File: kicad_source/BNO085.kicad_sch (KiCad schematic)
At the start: 16 parts, among them U4 BNO085, Y2 DNI

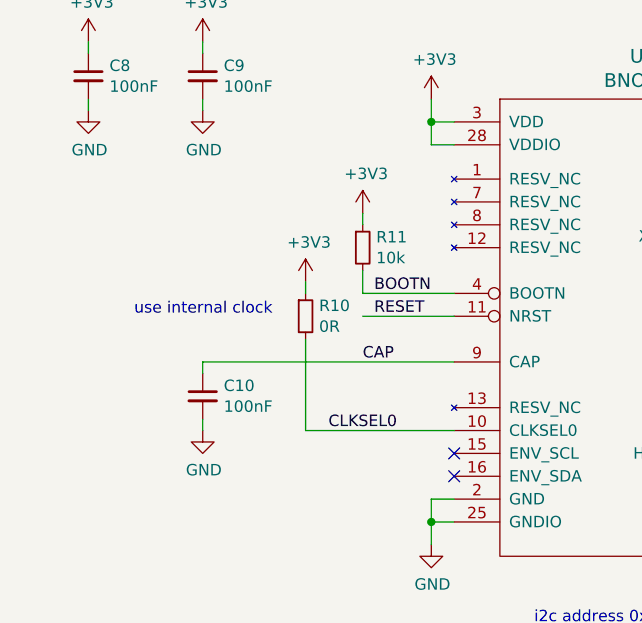
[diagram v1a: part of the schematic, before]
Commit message: connected reset of BNO055 and GNSS module, updated layout
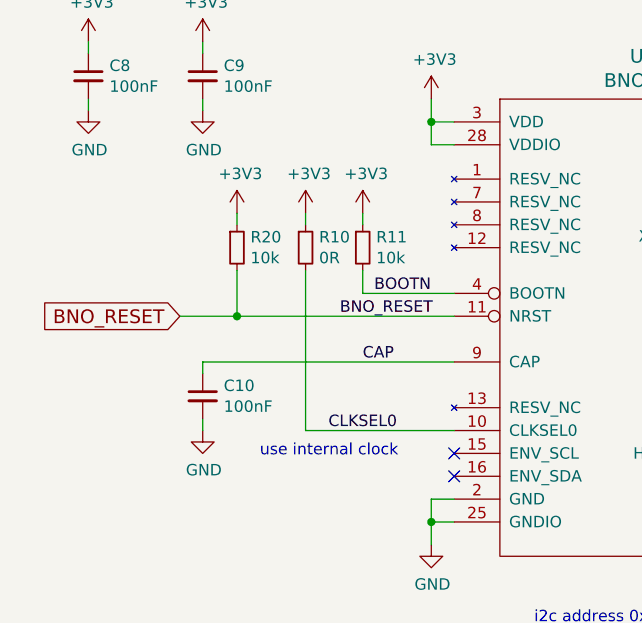
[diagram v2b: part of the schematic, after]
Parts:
- added R20: 10k, Resistor_SMD:R_0603_1608Metric, symbol NavShieldBNO-rescue:R_0603-devices
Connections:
- net +3V3: now also R20.1
- net RESET renamed BNO_RESET
- net BNO_RESET: now also R20.2
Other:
- moved on the sheet: R10
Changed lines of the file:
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@@
+	)
+	(junction
+		(at 39.37 54.61)
+		(diameter 0)
+		(color 0 0 0 0)
 	)
 	(junction
@@
 	(wire
 		(pts
+			(xy 39.37 49.53) (xy 39.37 54.61)
+		)
+		(stroke
+			(width 0)
+			(type default)
+		)
+	)
+	(wire
+		(pts
 			(xy 154.94 95.25) (xy 154.94 96.52)
 		)
@@
 	(wire
 		(pts
-			(xy 46.99 52.07) (xy 46.99 50.8)
+			(xy 46.99 44.45) (xy 46.99 43.18)
 		)
 		(stroke
@@
 	(wire
 		(pts
+			(xy 33.02 54.61) (xy 39.37 54.61)
+		)
+		(stroke
+			(width 0)
+			(type default)
+		)
+	)
+	(wire
+		(pts
 			(xy 140.97 59.69) (xy 140.97 72.39)
 		)
@@
 	(wire
 		(pts
+			(xy 39.37 54.61) (xy 63.5 54.61)
+		)
+		(stroke
+			(width 0)
+			(type default)
+		)
+	)
+	(wire
+		(pts
 			(xy 132.08 36.83) (xy 134.62 36.83)
 		)
@@
 	(wire
 		(pts
+			(xy 39.37 43.18) (xy 39.37 44.45)
+		)
+		(stroke
+			(width 0)
+			(type default)
+		)
+	)
+	(wire
+		(pts
 			(xy 154.94 101.6) (xy 154.94 102.87)
 		)
@@
 	(wire
 		(pts
-			(xy 53.34 54.61) (xy 63.5 54.61)
-		)
-		(stroke
-			(width 0)
-			(type default)
-		)
-	)
-	(wire
-		(pts
 			(xy 123.19 27.94) (xy 125.73 27.94)
 		)
@@
 	(wire
 		(pts
-			(xy 46.99 67.31) (xy 46.99 57.15)
+			(xy 46.99 49.53) (xy 46.99 67.31)
 		)
 		(stroke
@@
 	(text "use internal clock"
 		(exclude_from_sim no)
-		(at 27.94 54.61 0)
+		(at 41.91 70.358 0)
 		(effects
 			(font
@@
 		)
 	)
-	(label "RESET"
-		(at 54.61 54.61 0)
+	(label "BNO_RESET"
+		(at 50.8 54.61 0)
 		(effects
 			(font
@@
 		)
 	)
+	(global_label "BNO_RESET"
+		(shape input)
+		(at 33.02 54.61 180)
+		(fields_autoplaced yes)
+		(effects
+			(font
+				(size 1.524 1.524)
+			)
+			(justify right)
+		)
+		(property "Intersheetrefs" "${INTERSHEET_REFS}"
+			(at 17.4506 54.61 0)
+			(effects
+				(font
+					(size 1.27 1.27)
+				)
+				(justify right)
+				(hide yes)
+			)
+		)
+		(property "Referenzen zwischen Schaltplänen" "${INTERSHEET_REFS}"
+			(at 33.02 56.8121 0)
+			(effects
+				(font
+					(size 1.524 1.524)
+				)
+				(justify right)
+				(hide yes)
+			)
+		)
+	)
 	(symbol
 		(lib_id "NavShieldBNO-rescue:BNO085-MEMS")
@@
 	(symbol
 		(lib_id "NavShieldBNO-rescue:R_0603-devices")
-		(at 46.99 54.61 0)
+		(at 46.99 46.99 0)
 		(unit 1)
 		(exclude_from_sim no)
@@
 		(dnp no)
 		(property "Reference" "R10"
-			(at 48.4886 53.4416 0)
+			(at 48.4886 45.8216 0)
 			(effects
 				(font
@@
 		)
 		(property "Value" "0R"
-			(at 48.4886 55.753 0)
+			(at 48.4886 48.133 0)
 			(effects
 				(font
@@
 		)
 		(property "Footprint" "Resistor_SMD:R_0603_1608Metric"
-			(at 46.99 58.42 0)
-			(effects
-				(font
-					(size 1.27 1.27)
-				)
-				(hide yes)
-			)
-		)
-		(property "Datasheet" ""
-			(at 46.99 54.61 0)
-			(effects
-				(font
-					(size 1.27 1.27)
-				)
-			)
-		)
-		(property "Description" ""
-			(at 46.99 54.61 0)
+			(at 46.99 50.8 0)
+			(effects
+				(font
+					(size 1.27 1.27)
+				)
+				(hide yes)
+			)
+		)
+		(property "Datasheet" ""
+			(at 46.99 46.99 0)
+			(effects
+				(font
+					(size 1.27 1.27)
+				)
+			)
+		)
+		(property "Description" ""
+			(at 46.99 46.99 0)
 			(effects
 				(font
@@
 	)
 	(symbol
+		(lib_id "NavShieldBNO-rescue:R_0603-devices")
+		(at 39.37 46.99 0)
+		(unit 1)
+		(exclude_from_sim no)
+		(in_bom yes)
+		(on_board yes)
+		(dnp no)
+		(property "Reference" "R20"
+			(at 40.8686 45.8216 0)
+			(effects
+				(font
+					(size 1.27 1.27)
+				)
+				(justify left)
+			)
+		)
+		(property "Value" "10k"
+			(at 40.8686 48.133 0)
+			(effects
+				(font
+					(size 1.27 1.27)
+				)
+				(justify left)
+			)
+		)
+		(property "Footprint" "Resistor_SMD:R_0603_1608Metric"
+			(at 39.37 50.8 0)
+			(effects
+				(font
+					(size 1.27 1.27)
+				)
+				(hide yes)
+			)
+		)
+		(property "Datasheet" ""
+			(at 39.37 46.99 0)
+			(effects
+				(font
+					(size 1.27 1.27)
+				)
+			)
+		)
+		(property "Description" ""
+			(at 39.37 46.99 0)
+			(effects
+				(font
+					(size 1.27 1.27)
+				)
+				(hide yes)
+			)
+		)
+		(pin "1"
+		)
+		(pin "2"
+		)
+		(instances
+			(project "CyphalGNSSIMUBase-CAN"
+				(path "/9d6d512e-1439-4aa2-b0d9-afb2dddd9146/c16f48f1-b203-4e3b-a63b-33c1b1e484ca"
+					(reference "R20")
+					(unit 1)
+				)
+			)
+		)
+	)
+	(symbol
 		(lib_id "OpenCyphalPicoBase-rescue:+3.3V-power-supply")
 		(at 154.94 87.63 0)
@@
 	(symbol
 		(lib_id "OpenCyphalPicoBase-rescue:+3.3V-power-supply")
-		(at 46.99 50.8 0)
+		(at 46.99 43.18 0)
 		(unit 1)
 		(exclude_from_sim no)
@@
 		(dnp no)
 		(property "Reference" "#PWR43"
-			(at 46.99 54.61 0)
+			(at 46.99 46.99 0)
 			(effects
 				(font
@@
 		)
 		(property "Value" "+3V3"
-			(at 47.371 46.4058 0)
+			(at 47.371 38.7858 0)
 			(effects
 				(font
@@
 		)
 		(property "Footprint" ""
-			(at 46.99 50.8 0)
-			(effects
-				(font
-					(size 1.27 1.27)
-				)
-			)
-		)
-		(property "Datasheet" ""
-			(at 46.99 50.8 0)
-			(effects
-				(font
-					(size 1.27 1.27)
-				)
-			)
-		)
-		(property "Description" ""
-			(at 46.99 50.8 0)
+			(at 46.99 43.18 0)
+			(effects
+				(font
+					(size 1.27 1.27)
+				)
+			)
+		)
+		(property "Datasheet" ""
+			(at 46.99 43.18 0)
+			(effects
+				(font
+					(size 1.27 1.27)
+				)
+			)
+		)
+		(property "Description" ""
+			(at 46.99 43.18 0)
 			(effects
 				(font
@@
 					(unit 1)
 				)
+			)
+		)
+	)
+	(symbol
+		(lib_id "OpenCyphalPicoBase-rescue:+3.3V-power-supply")
+		(at 39.37 43.18 0)
+		(unit 1)
+		(exclude_from_sim no)
+		(in_bom yes)
+		(on_board yes)
+		(dnp no)
+		(property "Reference" "#PWR69"
+			(at 39.37 46.99 0)
+			(effects
+				(font
+					(size 1.27 1.27)
+				)
+				(hide yes)
+			)
+		)
+		(property "Value" "+3V3"
+			(at 39.751 38.7858 0)
+			(effects
+				(font
+					(size 1.27 1.27)
+				)
+			)
+		)
+		(property "Footprint" ""
+			(at 39.37 43.18 0)
+			(effects
+				(font
+					(size 1.27 1.27)
+				)
+			)
+		)
+		(property "Datasheet" ""
+			(at 39.37 43.18 0)
+			(effects
+				(font
+					(size 1.27 1.27)
+				)
+			)
+		)
+		(property "Description" ""
+			(at 39.37 43.18 0)
+			(effects
+				(font
+					(size 1.27 1.27)
+				)
+				(hide yes)
+			)
+		)
+		(pin "1"
+		)
+		(instances
+			(project "CyphalGNSSIMUBase-CAN"
+				(path "/9d6d512e-1439-4aa2-b0d9-afb2dddd9146/c16f48f1-b203-4e3b-a63b-33c1b1e484ca"
+					(reference "#PWR69")
+					(unit 1)
+				)
